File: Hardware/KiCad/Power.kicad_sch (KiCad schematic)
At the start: 10 parts, among them IC1 LM74502HDDFR, Q6 PSMN8R5-40MSDX

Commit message: revB
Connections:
- net at IC1.6 (GATE): no longer Q6.2 (G)
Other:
- moved on the sheet: Q6
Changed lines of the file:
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@@
 	)
 	(junction
-		(at 86.36 57.785)
+		(at 86.36 58.42)
 		(diameter 0)
 		(color 0 0 0 0)
@@
 	(wire
 		(pts
-			(xy 128.27 57.785) (xy 128.27 62.23)
+			(xy 128.27 58.42) (xy 128.27 62.23)
+		)
+		(stroke
+			(width 0)
+			(type default)
+		)
+	)
+	(wire
+		(pts
+			(xy 104.14 63.5) (xy 104.14 80.01)
+		)
+		(stroke
+			(width 0)
+			(type default)
+		)
+	)
+	(wire
+		(pts
+			(xy 128.27 62.23) (xy 128.27 80.01)
+		)
+		(stroke
+			(width 0)
+			(type default)
+		)
+	)
+	(wire
+		(pts
+			(xy 128.27 62.23) (xy 133.35 62.23)
+		)
+		(stroke
+			(width 0)
+			(type default)
+		)
+	)
+	(wire
+		(pts
+			(xy 86.36 101.6) (xy 95.25 101.6)
+		)
+		(stroke
+			(width 0)
+			(type default)
+		)
+	)
+	(wire
+		(pts
+			(xy 128.27 58.42) (xy 110.49 58.42)
+		)
+		(stroke
+			(width 0)
+			(type default)
+		)
+	)
+	(polyline
+		(pts
+			(xy 63.5 28.956) (xy 63.5 33.02)
+		)
+		(stroke
+			(width 0)
+			(type default)
+		)
+	)
+	(wire
+		(pts
+			(xy 86.36 57.15) (xy 86.36 58.42)
+		)
+		(stroke
+			(width 0)
+			(type default)
+		)
+	)
+	(wire
+		(pts
+			(xy 185.42 66.04) (xy 185.42 74.93)
+		)
+		(stroke
+			(width 0)
+			(type default)
+		)
+	)
+	(wire
+		(pts
+			(xy 86.36 92.71) (xy 95.25 92.71)
+		)
+		(stroke
+			(width 0)
+			(type default)
+		)
+	)
+	(wire
+		(pts
+			(xy 115.57 85.09) (xy 115.57 80.01)
+		)
+		(stroke
+			(width 0)
+			(type default)
+		)
+	)
+	(wire
+		(pts
+			(xy 175.26 66.04) (xy 175.26 74.93)
+		)
+		(stroke
+			(width 0)
+			(type default)
+		)
+	)
+	(wire
+		(pts
+			(xy 86.36 80.01) (xy 86.36 92.71)
+		)
+		(stroke
+			(width 0)
+			(type default)
+		)
+	)
+	(wire
+		(pts
+			(xy 99.06 58.42) (xy 86.36 58.42)
+		)
+		(stroke
+			(width 0)
+			(type default)
+		)
+	)
+	(polyline
+		(pts
+			(xy 35.306 33.02) (xy 63.5 33.02)
+		)
+		(stroke
+			(width 0)
+			(type default)
+		)
+	)
+	(wire
+		(pts
+			(xy 133.35 62.23) (xy 133.35 67.31)
+		)
+		(stroke
+			(width 0)
+			(type default)
+		)
+	)
+	(wire
+		(pts
+			(xy 86.36 100.33) (xy 86.36 101.6)
 		)
 		(stroke
@@
 	(wire
 		(pts
-			(xy 104.14 63.5) (xy 104.14 80.01)
-		)
-		(stroke
-			(width 0)
-			(type default)
-		)
-	)
-	(wire
-		(pts
-			(xy 128.27 62.23) (xy 128.27 80.01)
-		)
-		(stroke
-			(width 0)
-			(type default)
-		)
-	)
-	(wire
-		(pts
-			(xy 128.27 62.23) (xy 133.35 62.23)
-		)
-		(stroke
-			(width 0)
-			(type default)
-		)
-	)
-	(wire
-		(pts
-			(xy 86.36 101.6) (xy 95.25 101.6)
-		)
-		(stroke
-			(width 0)
-			(type default)
-		)
-	)
-	(wire
-		(pts
-			(xy 128.27 57.785) (xy 109.855 57.785)
-		)
-		(stroke
-			(width 0)
-			(type default)
-		)
-	)
-	(polyline
-		(pts
-			(xy 63.5 28.956) (xy 63.5 33.02)
-		)
-		(stroke
-			(width 0)
-			(type default)
-		)
-	)
-	(wire
-		(pts
-			(xy 86.36 57.15) (xy 86.36 57.785)
-		)
-		(stroke
-			(width 0)
-			(type default)
-		)
-	)
-	(wire
-		(pts
-			(xy 185.42 66.04) (xy 185.42 74.93)
-		)
-		(stroke
-			(width 0)
-			(type default)
-		)
-	)
-	(wire
-		(pts
-			(xy 86.36 92.71) (xy 95.25 92.71)
-		)
-		(stroke
-			(width 0)
-			(type default)
-		)
-	)
-	(wire
-		(pts
-			(xy 115.57 85.09) (xy 115.57 80.01)
-		)
-		(stroke
-			(width 0)
-			(type default)
-		)
-	)
-	(wire
-		(pts
-			(xy 175.26 66.04) (xy 175.26 74.93)
-		)
-		(stroke
-			(width 0)
-			(type default)
-		)
-	)
-	(wire
-		(pts
-			(xy 86.36 80.01) (xy 86.36 92.71)
-		)
-		(stroke
-			(width 0)
-			(type default)
-		)
-	)
-	(wire
-		(pts
-			(xy 98.425 57.785) (xy 86.36 57.785)
-		)
-		(stroke
-			(width 0)
-			(type default)
-		)
-	)
-	(polyline
-		(pts
-			(xy 35.306 33.02) (xy 63.5 33.02)
-		)
-		(stroke
-			(width 0)
-			(type default)
-		)
-	)
-	(wire
-		(pts
-			(xy 133.35 62.23) (xy 133.35 67.31)
-		)
-		(stroke
-			(width 0)
-			(type default)
-		)
-	)
-	(wire
-		(pts
-			(xy 86.36 100.33) (xy 86.36 101.6)
-		)
-		(stroke
-			(width 0)
-			(type default)
-		)
-	)
-	(wire
-		(pts
 			(xy 81.28 57.15) (xy 86.36 57.15)
 		)
@@
 	(wire
 		(pts
-			(xy 86.36 57.785) (xy 86.36 72.39)
+			(xy 86.36 58.42) (xy 86.36 72.39)
 		)
 		(stroke
@@
 	(hierarchical_label "VIN"
 		(shape input)
-		(at 76.2 57.15 180)
+		(at 72.39 57.15 180)
 		(effects
 			(font
@@
 	(symbol
 		(lib_id "utsvt_power:PSMN8R5-40MSDX")
-		(at 104.14 57.15 0)
+		(at 104.775 57.785 0)
 		(mirror y)
 		(unit 1)
@@
 		(fields_autoplaced yes)
 		(property "Reference" "Q6"
-			(at 104.14 49.53 0)
+			(at 104.775 50.165 0)
 			(effects
 				(font
@@
 		)
 		(property "Value" "PSMN8R5-40MSDX"
-			(at 104.14 52.07 0)
+			(at 104.775 52.705 0)
 			(effects
 				(font
@@
 		)
 		(property "Footprint" "UTSVT_Power:PSMN8R5-40MSDX"
-			(at 82.55 152.07 0)
+			(at 83.185 152.705 0)
 			(effects
 				(font
@@
 		)
 		(property "Datasheet" "https://assets.nexperia.com/documents/data-sheet/PSMN8R5-40MSD.pdf"
-			(at 82.55 252.07 0)
+			(at 83.185 252.705 0)
 			(effects
 				(font
@@
 		)
 		(property "Description" "MOSFETs PSMN8R5-40MSD/SOT1210/mLFPAK"
-			(at 103.124 45.72 0)
+			(at 103.759 46.355 0)
 			(effects
 				(font
@@
 		)
 		(property "Height" "1"
-			(at 82.55 452.07 0)
+			(at 83.185 452.705 0)
 			(effects
 				(font
@@
 		)
 		(property "Mouser Part Number" "771-PSMN8R5-40MSDX"
-			(at 82.55 552.07 0)
+			(at 83.185 552.705 0)
 			(effects
 				(font
@@
 		)
 		(property "Mouser Price/Stock" "https://www.mouser.co.uk/ProductDetail/Nexperia/PSMN8R5-40MSDX?qs=vHuUswq2%252BswjdnYdBdHaPw%3D%3D"
-			(at 82.55 652.07 0)
+			(at 83.185 652.705 0)
 			(effects
 				(font
@@
 		)
 		(property "Manufacturer_Name" "Nexperia"
-			(at 82.55 752.07 0)
+			(at 83.185 752.705 0)
 			(effects
 				(font
@@
 		)
 		(property "Manufacturer_Part_Number" "PSMN8R5-40MSDX"
-			(at 82.55 852.07 0)
+			(at 83.185 852.705 0)
 			(effects
 				(font
@@
 		)
 		(property "Sim.Type" ""
-			(at 104.14 57.15 0)
+			(at 104.775 57.785 0)
 			(effects
 				(font
@@
 		)
 		(property "Description (Customer #)" ""
-			(at 104.14 57.15 0)
-			(effects
-				(font
+			(at 104.775 57.785 0)
+			(effects
+				(font

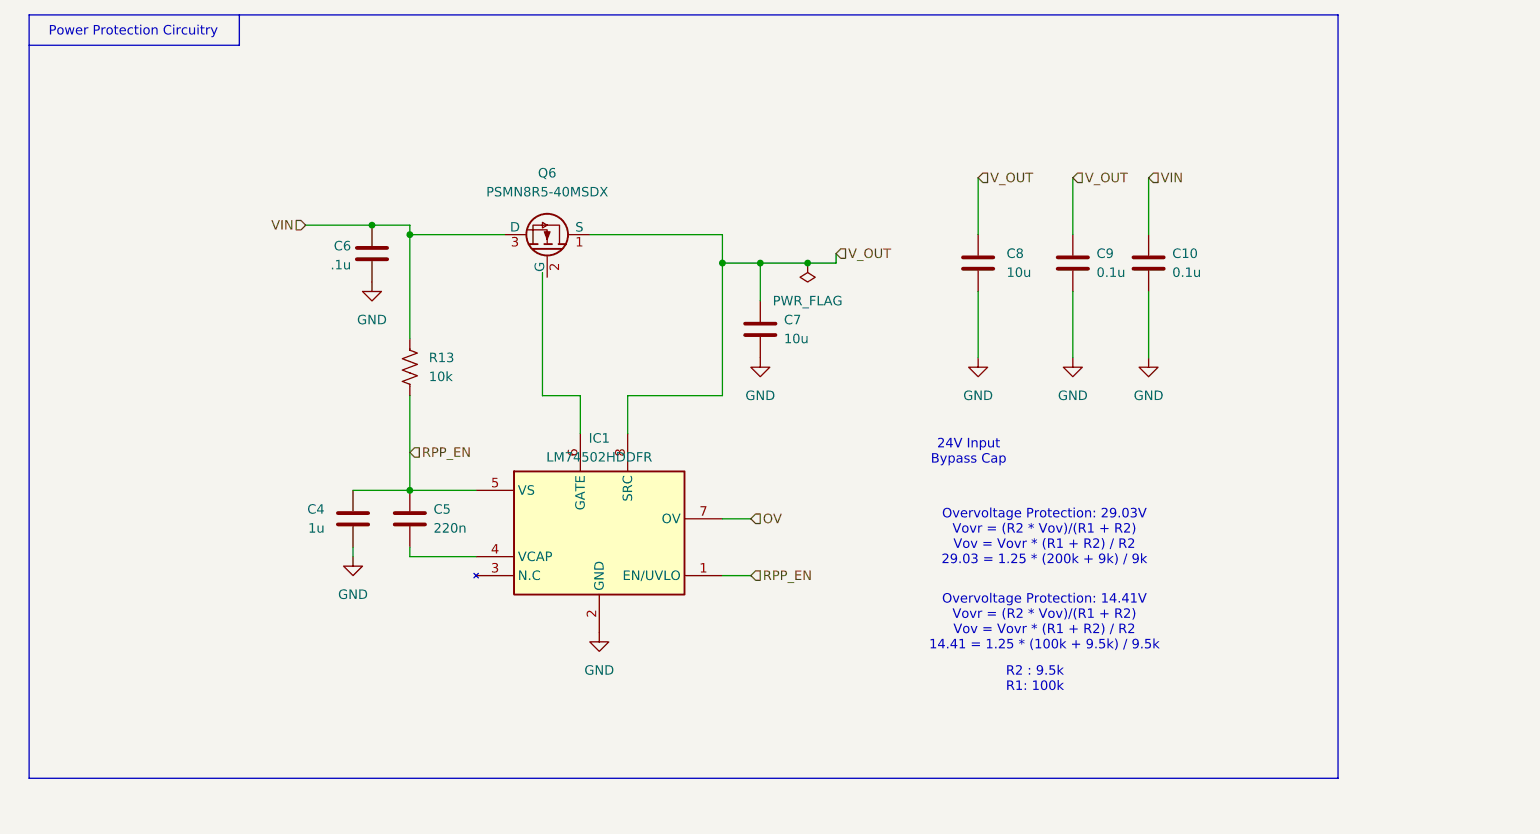
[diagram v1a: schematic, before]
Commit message: schematic changes, pre pcb revB changes
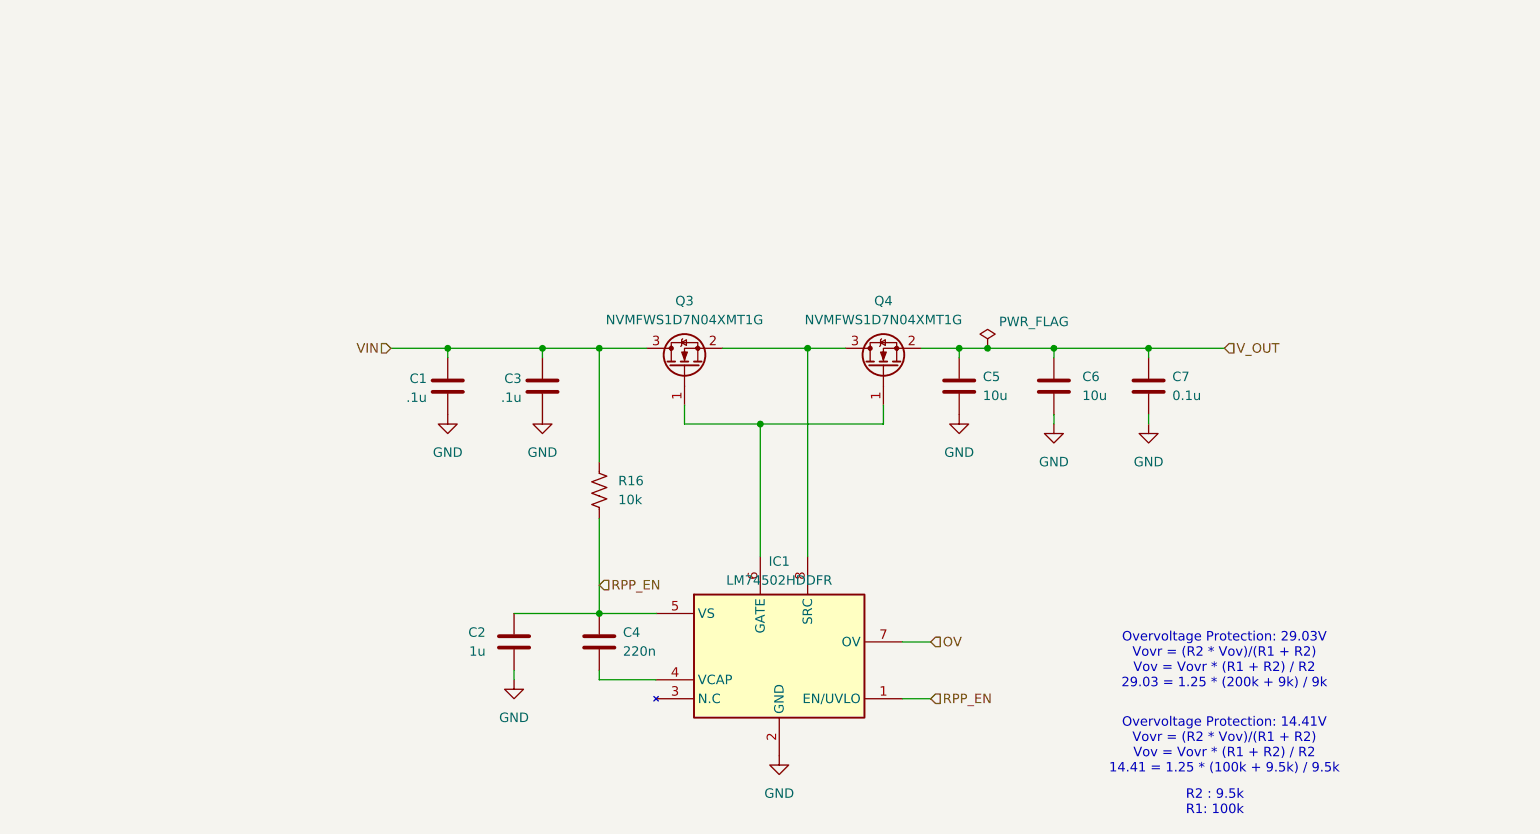
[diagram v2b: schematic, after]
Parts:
- removed C10: 0.1u, Capacitor_SMD:C_0603_1608Metric_Pad1.08x0.95mm_HandSolder, symbol Device:C
- removed Q6: PSMN8R5-40MSDX, UTSVT_Power:PSMN8R5-40MSDX, symbol utsvt_power:PSMN8R5-40MSDX
- added C3: .1u, Capacitor_SMD:C_0603_1608Metric_Pad1.08x0.95mm_HandSolder, symbol Device:C
- added Q3, Q4: NVMFWS1D7N04XMT1G, Package_TO_SOT_SMD:SOT-23, symbol Transistor_FET:IRLML0030
- C1: renamed from C6; LCSC (none) -> C14663
- C2: renamed from C4; LCSC (none) -> C15849
- C4: renamed from C5; LCSC (none) -> C344195
- C5: renamed from C7; LCSC (none) -> C440198
- C6: renamed from C8; LCSC (none) -> C440198
- C7: renamed from C9; LCSC (none) -> C14663
- IC1: LCSC (none) -> C5219202
- R16: renamed from R13; footprint Resistor_SMD:R_0603_1608Metric_Pad0.98x0.95mm_HandSolder -> Resistor_SMD:R_0805_2012Metric_Pad1.20x1.40mm_HandSolder
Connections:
- net GND: now also C3.1
- net VIN: now also C3.2, Q3.3 (D)
- net V_OUT: now also Q4.2 (S); no longer IC1.8 (SRC)
- net at IC1.6 (GATE): now also Q3.1 (G), Q4.1 (G)
- new net: IC1.8 (SRC), Q3.2 (S), Q4.3 (D)
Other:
- note removed: "24V Input Bypass Cap"
- note removed: "Power Protection Circuitry"
- moved on the sheet: C1, C2, C4, C5, C6, C7, IC1, R16

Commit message: sch changes, pre pcb changes
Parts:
- removed Q3, Q4: NVMFWS1D7N04XMT1G, Package_TO_SOT_SMD:SOT-23, symbol Transistor_FET:IRLML0030
- added Q3, Q4: NVMFWS1D7N04XMT1G, UTSVT_Power:NVMFWS3D0P04M8LT1G, symbol UTSVT_Misc:NVMFWS1D7N04XMT1G
- added R13: 100k, Resistor_SMD:R_0603_1608Metric_Pad0.98x0.95mm_HandSolder, symbol Device:R_US
- added R14: 9。5k, Resistor_SMD:R_0603_1608Metric_Pad0.98x0.95mm_HandSolder, symbol Device:R_US
- added Z2: SMAF4758A, UTSVT_Passives:SODFL5026X125N, symbol UTSVT_Power:SMAF4749A-TP
- renumbered R16 to R12
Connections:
- net GND: now also R14.1, Z2.2 (A)
- net RPP_EN: now also Z2.1 (K)
- net VIN: now also Q3.5, Q3.6, Q3.7, Q3.8, Q3.9, R13.1
- net at IC1.6 (GATE): now also Q3.4, Q4.4
- net at IC1.8 (SRC): now also Q3.1, Q3.2, Q3.3, Q4.5, Q4.6, Q4.7, Q4.8, Q4.9
- net OV: no longer names the net of IC1.7 (OV)
- net OV: now also R13.2, R14.2
- net V_OUT renamed VOUT
- net VOUT: now also Q4.1, Q4.2, Q4.3
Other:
- note added: "NZV: 56V"
- moved on the sheet: C1, C2, C3, C4, C5, C6, C7, R12

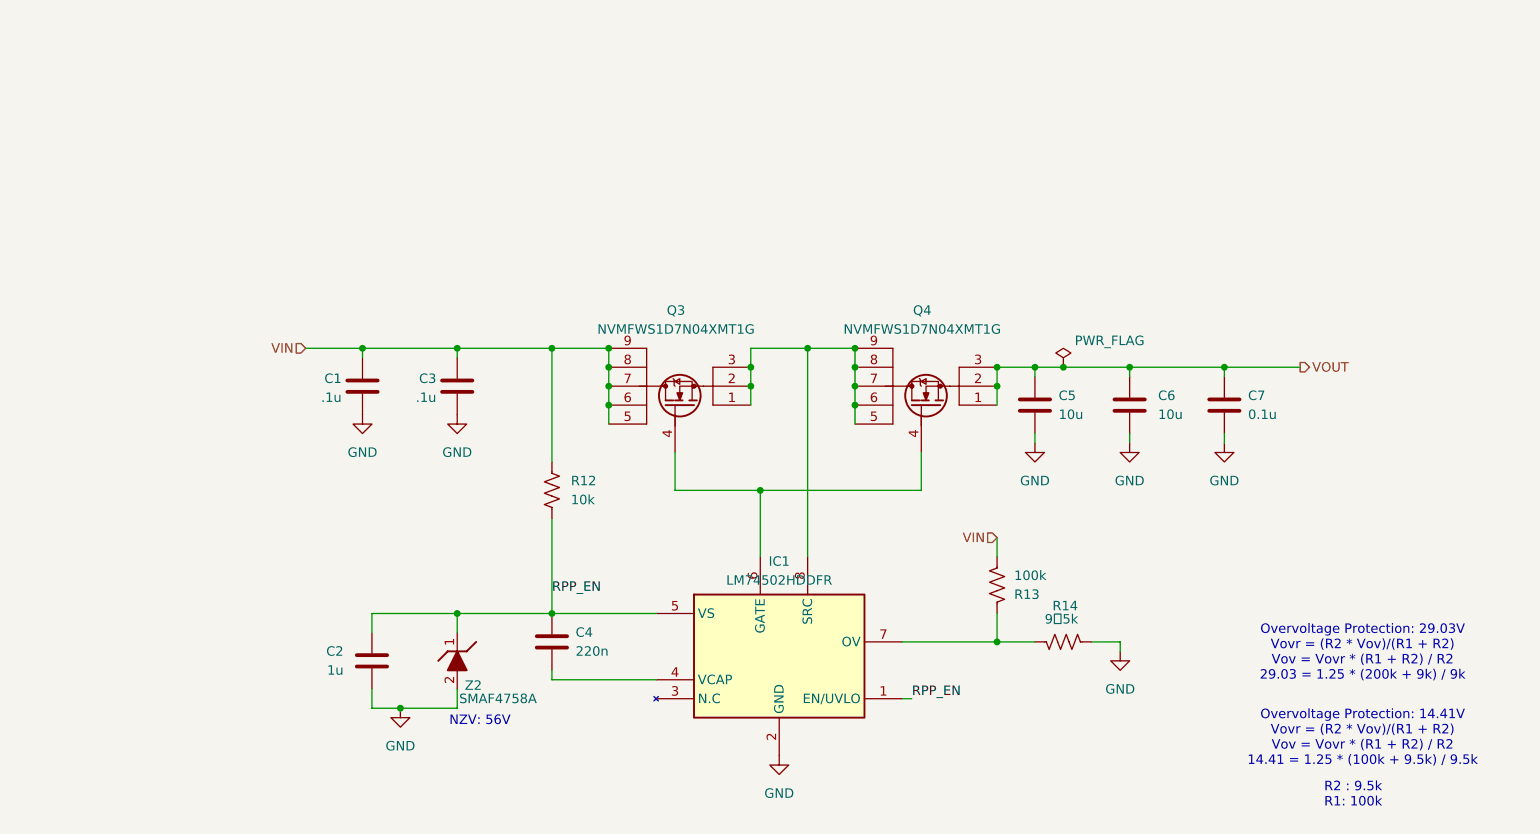
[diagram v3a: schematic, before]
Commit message: layout ready for review
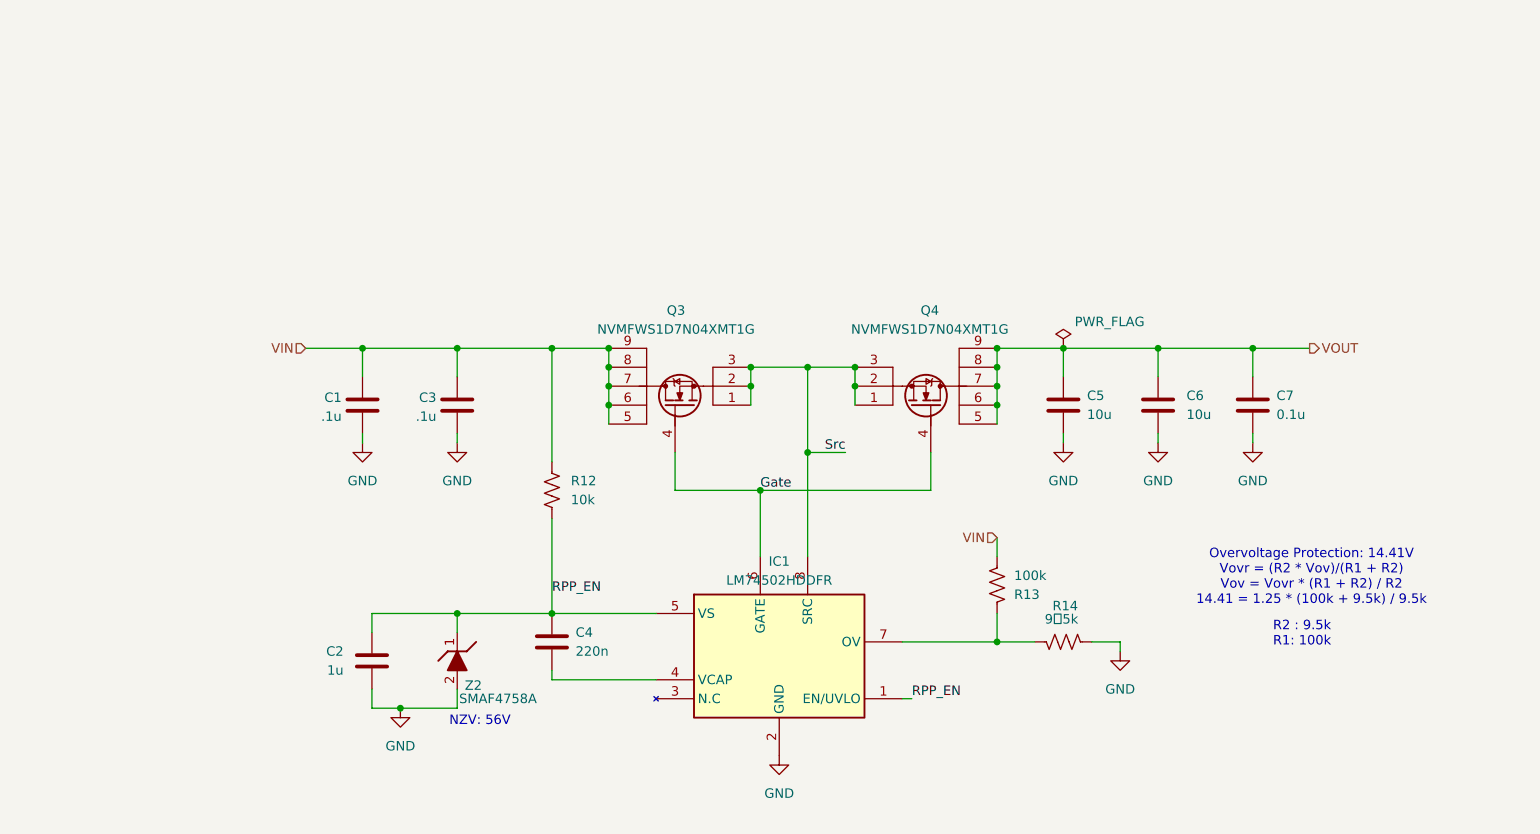
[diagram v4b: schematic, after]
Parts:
- C5, C6: footprint Capacitor_SMD:C_0805_2012Metric_Pad1.18x1.45mm_HandSolder -> Capacitor_SMD:C_0603_1608Metric_Pad1.08x0.95mm_HandSolder
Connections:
- net VOUT: now also Q4.5, Q4.6, Q4.7, Q4.8, Q4.9; no longer Q4.1, Q4.2, Q4.3
- net Gate: now reaches IC1.6 (GATE), Q3.4, Q4.4
- new net Src: IC1.8 (SRC), Q3.1, Q3.2, Q3.3, Q4.1, Q4.2, Q4.3
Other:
- note removed: "Overvoltage Protection: 29.03V Vovr = (R2 * Vov)/(R1 + R2) Vov = Vovr * (R1 + R2) / R2 29.03 = 1.25 * (200k + 9k) / 9k"
- moved on the sheet: C1, C3, C5, C6, C7, Q4

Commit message: done with changes
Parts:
- R12, R13, R14: symbol Device:R_US -> Device:R
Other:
- note added: "Moco CAN bus supply voltage maximum: 15V Recommended 13.8V"
- moved on the sheet: C2, C4, C5, C6, C7, Z2

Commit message: finished LCSC
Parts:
- C5, C6: LCSC C440198 -> C1691
- Q3, Q4: LCSC (none) -> C133142
- R12: LCSC (none) -> C702829
- R14: now left out of the parts list
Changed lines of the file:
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@@
 			)
 		)
-		(property "LCSC" ""
+		(property "LCSC" "C702829"
 			(at 105.41 91.44 0)
 			(effects
@@
 		(unit 1)
 		(exclude_from_sim no)
-		(in_bom yes)
+		(in_bom no)
 		(on_board yes)
 		(dnp no)
@@
 			)
 		)
+		(property "LCSC" "C133142"
+			(at 156.21 80.01 90)
+			(effects
+				(font
+					(size 1.27 1.27)
+				)
+				(hide yes)
+			)
+		)
 		(pin "1"
 		)
@@
 			)
 		)
+		(property "LCSC" "C133142"
+			(at 121.92 80.01 90)
+			(effects
+				(font
+					(size 1.27 1.27)
+				)
+				(hide yes)
+			)
+		)
 		(pin "1"
 		)
@@
 			)
 		)
-		(property "LCSC" "C440198"
+		(property "LCSC" "C1691"
 			(at 176.53 81.28 0)
 			(effects
@@
 			)
 		)
-		(property "LCSC" "C440198"
+		(property "LCSC" "C1691"
 			(at 189.23 81.28 0)
 			(effects
